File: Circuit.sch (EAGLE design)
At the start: 115 parts, among them IC1 LM1117T-3.3-V, P1 RASPI-P1RASPI_REV2_P1, P5 RASPI_P5

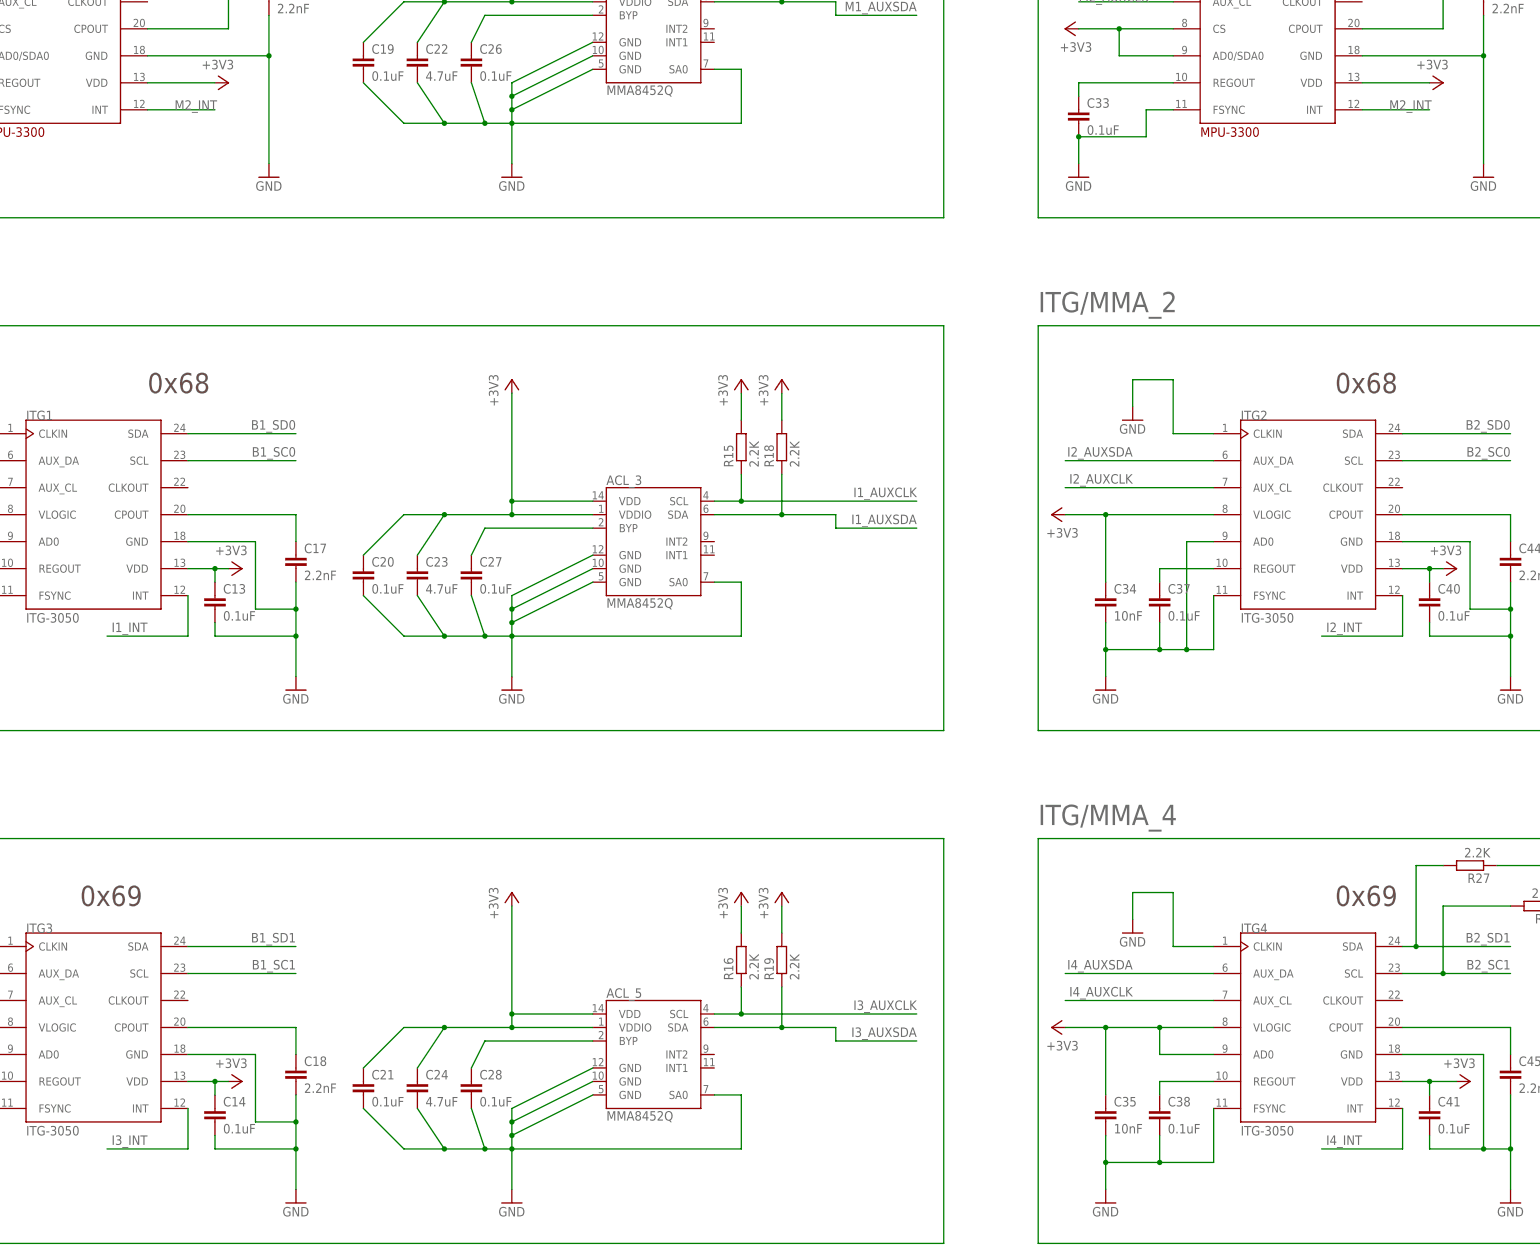
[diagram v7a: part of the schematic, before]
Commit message: Rearranging buses
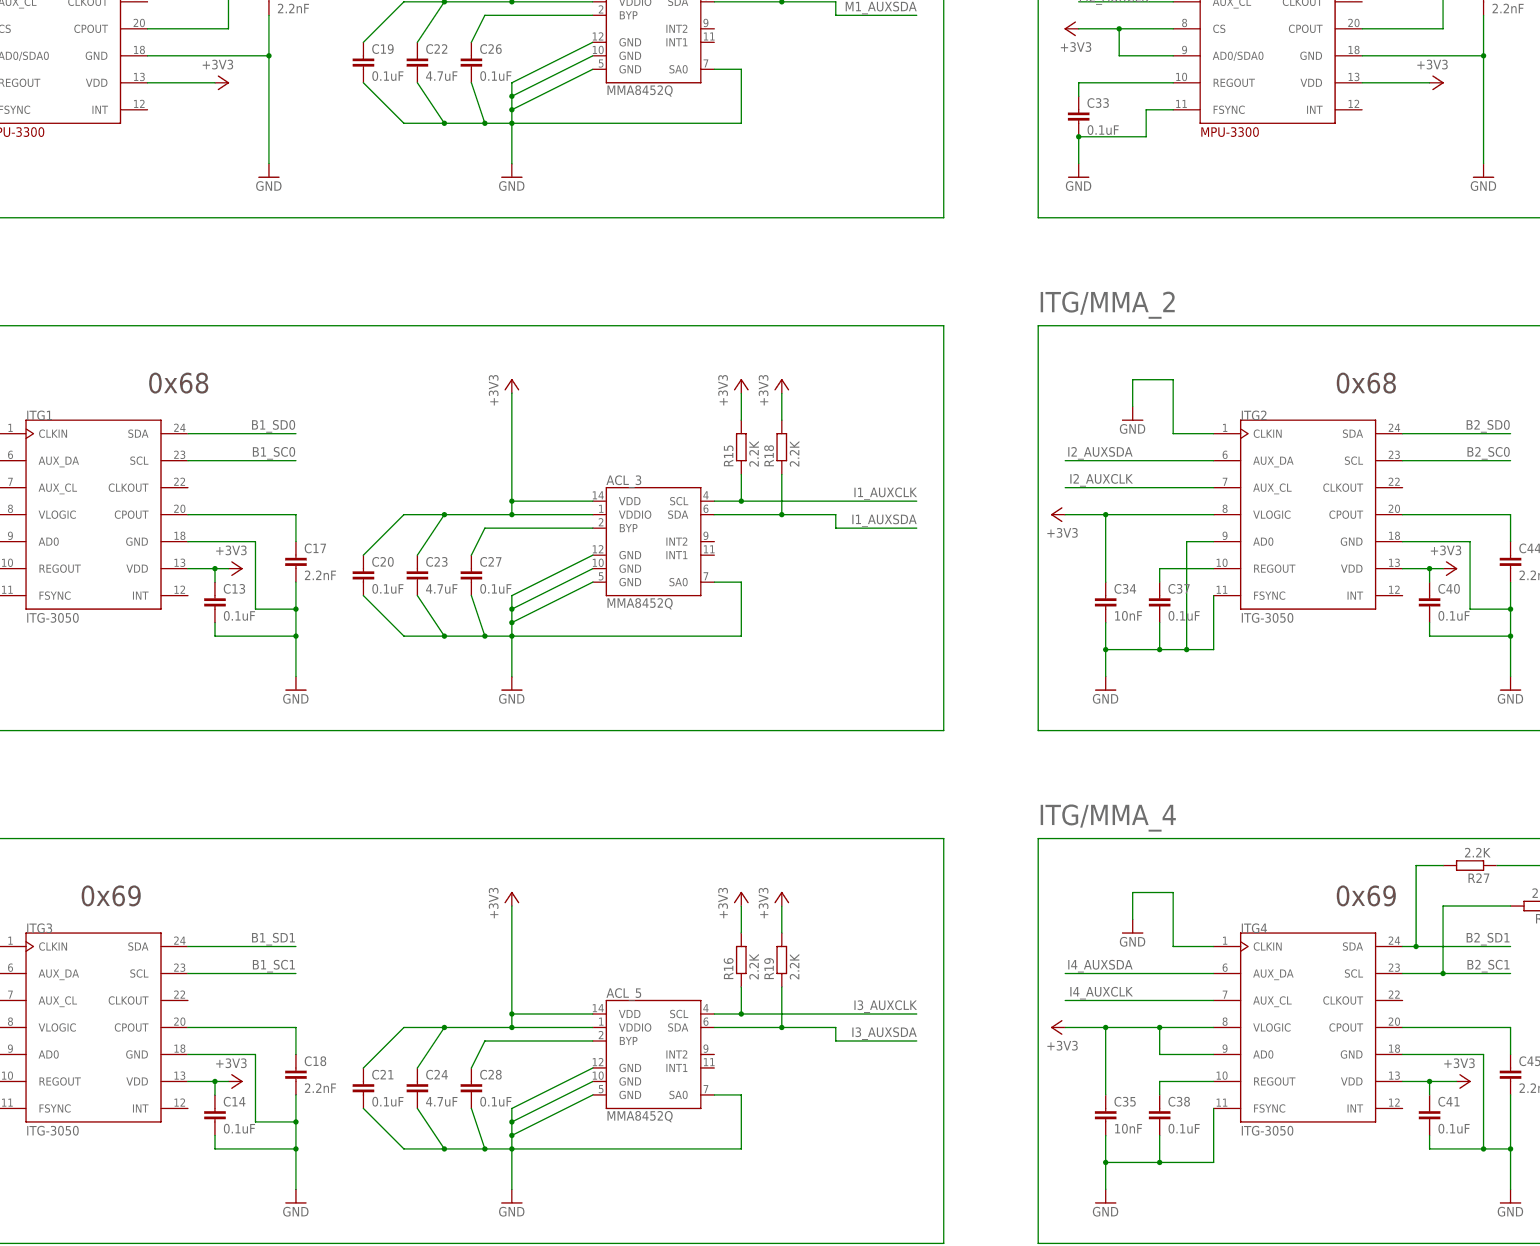
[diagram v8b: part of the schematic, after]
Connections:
- removed net I1_INT: ITG1.INT
- removed net I2_INT: ITG2.INT
- removed net I3_INT: ITG3.INT
- removed net I4_INT: ITG4.INT
- removed net M2_INT: MPU1.INT, MPU2.INT
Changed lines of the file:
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@@
-</segment>
-</net>
-<net name="M2_INT" class="0">
-<segment>
-<pinref part="MPU1" gate="G$1" pin="INT"/>
-<wire x1="-40.64" y1="302.26" x2="-27.94" y2="302.26" width="0.1524" layer="91"/>
-<label x="-35.56" y="302.26" size="1.778" layer="95"/>
-</segment>
-<segment>
-<pinref part="MPU2" gate="G$1" pin="INT"/>
-<wire x1="187.96" y1="302.26" x2="200.66" y2="302.26" width="0.1524" layer="91"/>
-<label x="193.04" y="302.26" size="1.778" layer="95"/>
 </segment>
 </net>
@@
 </segment>
 </net>
-<net name="I1_INT" class="0">
-<segment>
-<pinref part="ITG1" gate="G$1" pin="INT"/>
-<wire x1="-33.02" y1="210.82" x2="-33.02" y2="203.2" width="0.1524" layer="91"/>
-<wire x1="-33.02" y1="203.2" x2="-48.26" y2="203.2" width="0.1524" layer="91"/>
-<label x="-40.64" y="205.74" size="1.778" layer="95" rot="R180"/>
-</segment>
-</net>
 <net name="N$15" class="0">
 <segment>
@@
 </segment>
 </net>
-<net name="I2_INT" class="0">
-<segment>
-<pinref part="ITG2" gate="G$1" pin="INT"/>
-<wire x1="195.58" y1="210.82" x2="195.58" y2="203.2" width="0.1524" layer="91"/>
-<wire x1="195.58" y1="203.2" x2="180.34" y2="203.2" width="0.1524" layer="91"/>
-<label x="187.96" y="205.74" size="1.778" layer="95" rot="R180"/>
-</segment>
-</net>
 <net name="N$23" class="0">
 <segment>
@@
 </segment>
 </net>
-<net name="I3_INT" class="0">
-<segment>
-<pinref part="ITG3" gate="G$1" pin="INT"/>
-<wire x1="-33.02" y1="114.3" x2="-33.02" y2="106.68" width="0.1524" layer="91"/>
-<wire x1="-33.02" y1="106.68" x2="-48.26" y2="106.68" width="0.1524" layer="91"/>
-<label x="-40.64" y="109.22" size="1.778" layer="95" rot="R180"/>
-</segment>
-</net>
 <net name="N$30" class="0">
 <segment>
@@
 </segment>
 </net>
-<net name="I4_INT" class="0">
-<segment>
-<pinref part="ITG4" gate="G$1" pin="INT"/>
-<wire x1="195.58" y1="114.3" x2="195.58" y2="106.68" width="0.1524" layer="91"/>
-<wire x1="195.58" y1="106.68" x2="180.34" y2="106.68" width="0.1524" layer="91"/>
-<label x="187.96" y="109.22" size="1.778" layer="95" rot="R180"/>
-</segment>
-</net>
